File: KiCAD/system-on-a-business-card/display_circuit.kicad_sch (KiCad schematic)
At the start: 12 parts, among them J2 X077-6428TSWCG01-H13, Q1 2N7002K, Q2 BSS84

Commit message: updated documentation, fixed bom export
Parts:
- J2: now in the parts list
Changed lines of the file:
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@@
   )
   (symbol (lib_id "Connector:Conn_01x13_Male") (at 227.33 80.01 0) (mirror y) (unit 1)
-    (in_bom no) (on_board yes)
+    (in_bom yes) (on_board yes)
     (property "Reference" "J2" (id 0) (at 229.87 80.01 0)
       (effects (font (size 1.27 1.27)) (justify right))

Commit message: fixed #12 connected OLED VDD pins to 3.3V power line
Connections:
- net +3.3V: now reaches C19.1, C21.1, J2.4 (Pin_4), J2.5 (Pin_5)

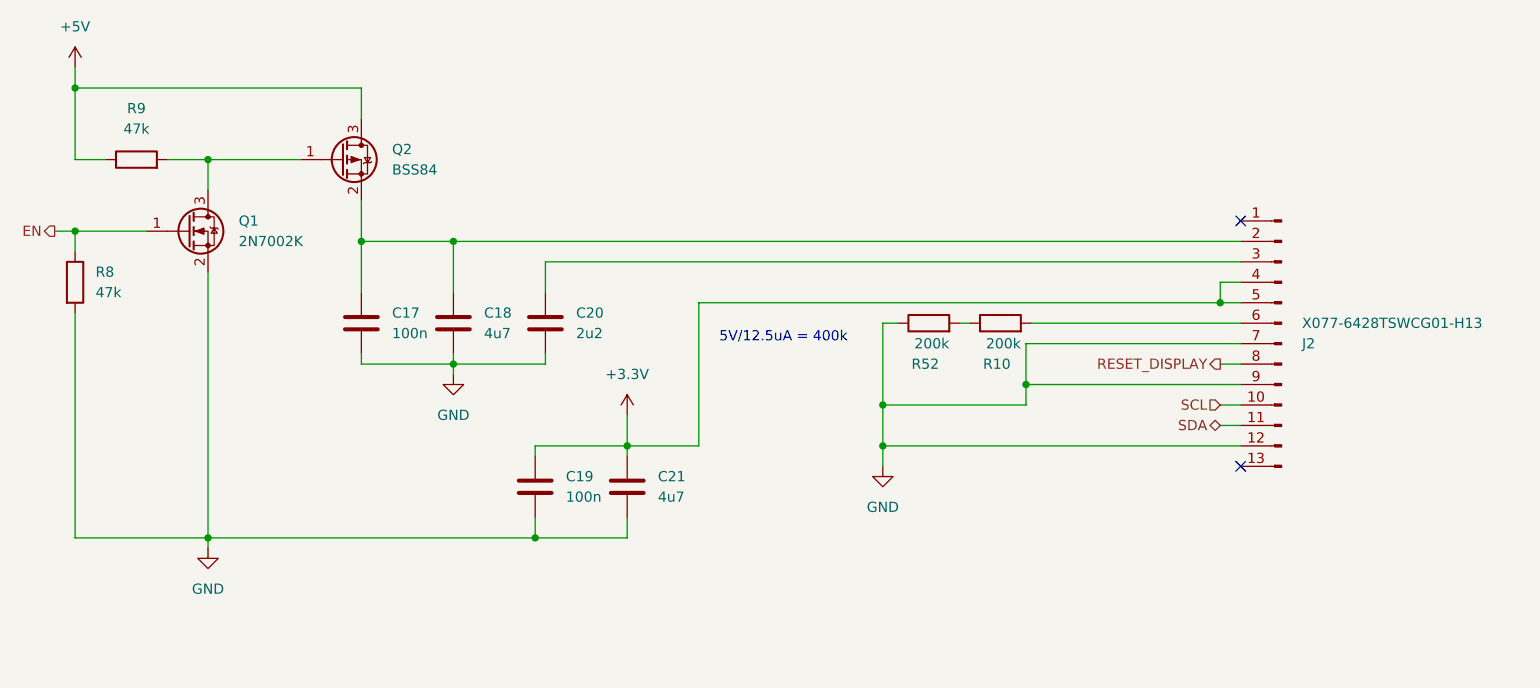
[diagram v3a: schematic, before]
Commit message: #10: added buzzer, io-expander, removed transistors from resistive pad cirucit
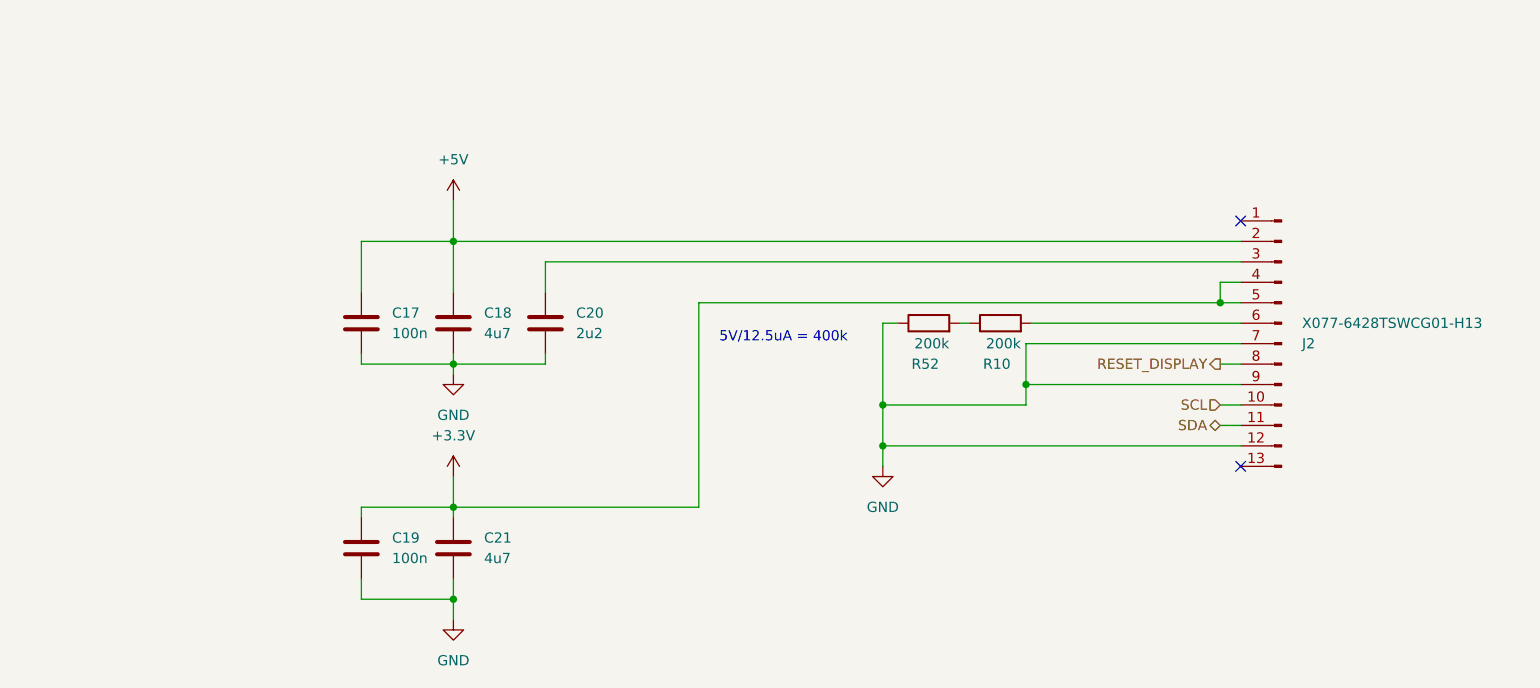
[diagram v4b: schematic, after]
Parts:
- removed Q1: 2N7002K, Package_TO_SOT_SMD:SOT-23, symbol Transistor_FET:2N7002K
- removed Q2: BSS84, Package_TO_SOT_SMD:SOT-23, symbol Transistor_FET:BSS84
- removed R8, R9: 47k, Resistor_SMD:R_0402_1005Metric_Pad0.72x0.64mm_HandSolder, symbol Device:R
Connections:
- net +5V: now also C17.1, C18.1, J2.2 (Pin_2)
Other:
- moved on the sheet: C19, C21

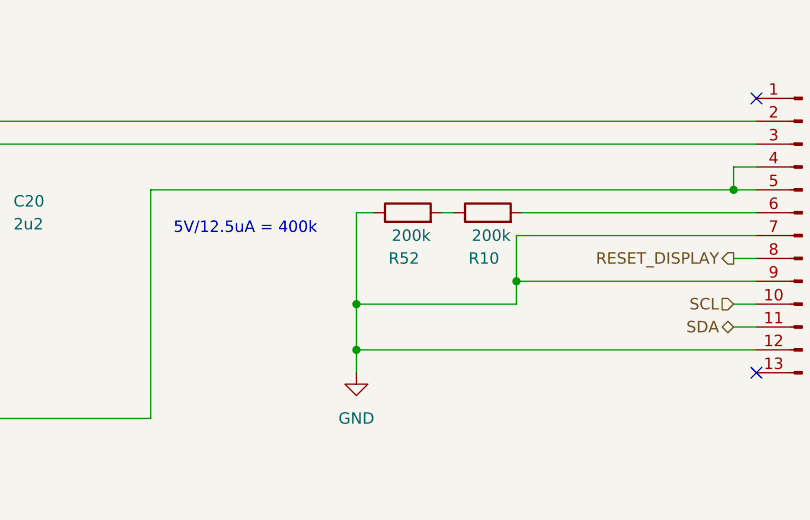
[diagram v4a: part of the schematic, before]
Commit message: #10: removed on/off switch again, started working on layout
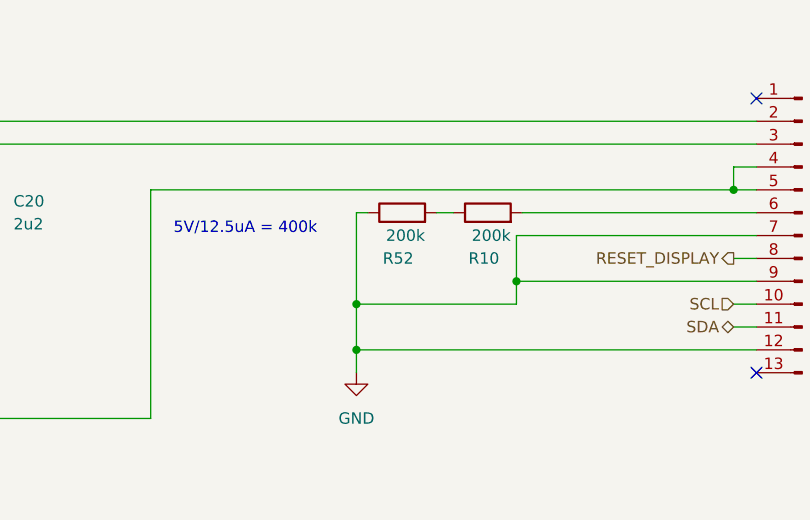
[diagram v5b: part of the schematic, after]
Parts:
- J2: symbol Connector:Conn_01x13_Male -> Connector:Conn_01x13_Pin
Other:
- moved on the sheet: R52
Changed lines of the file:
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@@
     (stroke (width 0) (type default))
   )
-  (wire (pts (xy 177.8 77.47) (xy 179.705 77.47))
+  (wire (pts (xy 177.8 77.47) (xy 179.07 77.47))
     (stroke (width 0) (type default))
   )
@@
     (stroke (width 0) (type default))
   )
-  (wire (pts (xy 187.325 77.47) (xy 188.595 77.47))
+  (wire (pts (xy 186.69 77.47) (xy 188.595 77.47))
     (stroke (width 0) (type default))
   )
@@
     )
   )
-  (symbol (lib_id "Connector:Conn_01x13_Male") (at 227.33 80.01 0) (mirror y) (unit 1)
+  (symbol (lib_id "Connector:Conn_01x13_Pin") (at 227.33 80.01 0) (mirror y) (unit 1)
     (in_bom yes) (on_board yes) (dnp no)
     (property "Reference" "J2" (at 229.87 80.01 0)
@@
     )
   )
-  (symbol (lib_id "Device:R") (at 183.515 77.47 90) (unit 1)
+  (symbol (lib_id "Device:R") (at 182.88 77.47 90) (unit 1)
     (in_bom yes) (on_board yes) (dnp no)
-    (property "Reference" "R52" (at 184.785 82.55 90)
-      (effects (font (size 1.27 1.27)) (justify left))
-    )
-    (property "Value" "200k" (at 186.055 80.01 90)
-      (effects (font (size 1.27 1.27)) (justify left))
-    )
-    (property "Footprint" "Resistor_SMD:R_0402_1005Metric_Pad0.72x0.64mm_HandSolder" (at 183.515 79.248 90)
-      (effects (font (size 1.27 1.27)) hide)
-    )
-    (property "Datasheet" "~" (at 183.515 77.47 0)
-      (effects (font (size 1.27 1.27)) hide)
-    )
+    (property "Reference" "R52" (at 184.15 82.55 90)
+      (effects (font (size 1.27 1.27)) (justify left))
+    )
+    (property "Value" "200k" (at 185.42 80.01 90)
+      (effects (font (size 1.27 1.27)) (justify left))
+    )
+    (property "Footprint" "Resistor_SMD:R_0402_1005Metric_Pad0.72x0.64mm_HandSolder" (at 182.88 79.248 90)
+      (effects (font (size 1.27 1.27)) hide)
+    )
+    (property "Datasheet" "~" (at 182.88 77.47 0)
+      (effects (font (size 1.27 1.27)) hide)
+    )

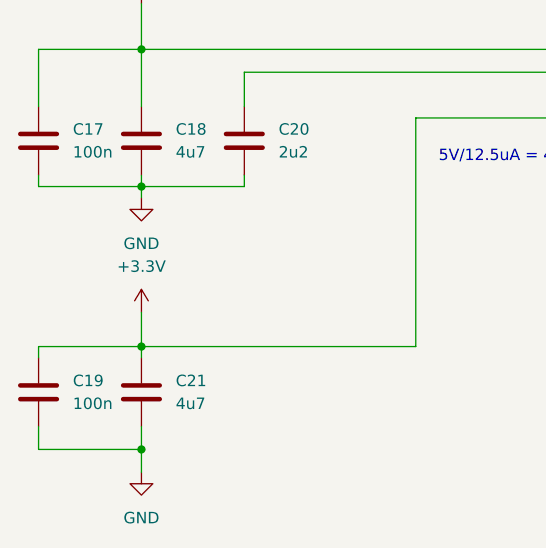
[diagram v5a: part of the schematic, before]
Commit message: #10: mintor tweaks in routing, removed fiducials from bom, added values to buzzer and sd-card slot
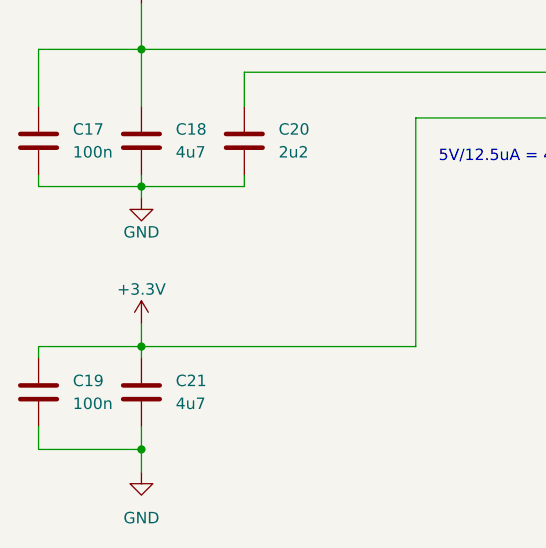
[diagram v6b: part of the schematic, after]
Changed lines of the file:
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@@
     (stroke (width 0) (type default))
   )
-  (wire (pts (xy 124.46 96.52) (xy 124.46 100.33))
+  (wire (pts (xy 124.46 97.79) (xy 124.46 100.33))
     (stroke (width 0) (type default))
   )
@@
   )
   (symbol (lib_id "power:GND") (at 124.46 83.82 0) (unit 1)
-    (in_bom yes) (on_board yes) (dnp no) (fields_autoplaced)
+    (in_bom yes) (on_board yes) (dnp no)
     (property "Reference" "#PWR024" (at 124.46 90.17 0)
       (effects (font (size 1.27 1.27)) hide)
     )
-    (property "Value" "GND" (at 124.46 88.9 0)
+    (property "Value" "GND" (at 124.46 87.63 0)
       (effects (font (size 1.27 1.27)))
     )
@@
     )
   )
-  (symbol (lib_id "power:+3.3V") (at 124.46 96.52 0) (unit 1)
-    (in_bom yes) (on_board yes) (dnp no)
-    (property "Reference" "#PWR04" (at 124.46 100.33 0)
-      (effects (font (size 1.27 1.27)) hide)
-    )
-    (property "Value" "+3.3V" (at 124.46 91.44 0)
+  (symbol (lib_id "power:+3.3V") (at 124.46 97.79 0) (unit 1)
+    (in_bom yes) (on_board yes) (dnp no)
+    (property "Reference" "#PWR04" (at 124.46 101.6 0)
+      (effects (font (size 1.27 1.27)) hide)
+    )
+    (property "Value" "+3.3V" (at 124.46 93.98 0)
       (effects (font (size 1.27 1.27)))
     )
-    (property "Footprint" "" (at 124.46 96.52 0)
-      (effects (font (size 1.27 1.27)) hide)
-    )
-    (property "Datasheet" "" (at 124.46 96.52 0)
-      (effects (font (size 1.27 1.27)) hide)
-    )
+    (property "Footprint" "" (at 124.46 97.79 0)
+      (effects (font (size 1.27 1.27)) hide)
+    )
+    (property "Datasheet" "" (at 124.46 97.79 0)
+      (effects (font (size 1.27 1.27)) hide)
+    )

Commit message: #10: separated reset and display reset signals, added pull-up to display reset
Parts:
- added R5: 5k1, Resistor_SMD:R_0402_1005Metric_Pad0.72x0.64mm_HandSolder, symbol Device:R
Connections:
- net +3.3V: now also R5.1
- net RESET_DISPLAY: now also R5.2
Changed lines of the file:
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@@
   (junction (at 124.46 111.76) (diameter 0) (color 0 0 0 0)
   )
+  (junction (at 154.94 100.33) (diameter 0) (color 0 0 0 0)
+  )
   (junction (at 124.46 82.55) (diameter 0) (color 0 0 0 0)
   )
@@
   )
   (junction (at 124.46 100.33) (diameter 0) (color 0 0 0 0)
+  )
+  (junction (at 154.94 111.76) (diameter 0) (color 0 0 0 0)
   )
   (junction (at 177.8 92.71) (diameter 0) (color 0 0 0 0)
@@
   (no_connect (at 222.25 95.25))
   (no_connect (at 222.25 64.77))
-  (wire (pts (xy 154.94 100.33) (xy 124.46 100.33))
-    (stroke (width 0) (type default))
-  )
   (wire (pts (xy 135.89 69.85) (xy 222.25 69.85))
     (stroke (width 0) (type default))
@@
     (stroke (width 0) (type default))
   )
+  (wire (pts (xy 154.94 111.76) (xy 154.94 110.49))
+    (stroke (width 0) (type default))
+  )
   (wire (pts (xy 113.03 109.22) (xy 113.03 111.76))
     (stroke (width 0) (type default))
@@
     (stroke (width 0) (type default))
   )
+  (wire (pts (xy 124.46 100.33) (xy 154.94 100.33))
+    (stroke (width 0) (type default))
+  )
   (wire (pts (xy 177.8 92.71) (xy 222.25 92.71))
     (stroke (width 0) (type default))
@@
     (stroke (width 0) (type default))
   )
+  (wire (pts (xy 154.94 111.76) (xy 160.02 111.76))
+    (stroke (width 0) (type default))
+  )
   (wire (pts (xy 222.25 80.01) (xy 195.58 80.01))
     (stroke (width 0) (type default))
@@
     (stroke (width 0) (type default))
   )
+  (wire (pts (xy 149.86 111.76) (xy 154.94 111.76))
+    (stroke (width 0) (type default))
+  )
   (wire (pts (xy 195.58 85.09) (xy 222.25 85.09))
     (stroke (width 0) (type default))
@@
   )
   (wire (pts (xy 124.46 62.23) (xy 124.46 67.31))
+    (stroke (width 0) (type default))
+  )
+  (wire (pts (xy 154.94 102.87) (xy 154.94 100.33))
     (stroke (width 0) (type default))
   )
@@
     (effects (font (size 1.27 1.27)) (justify left bottom))
   )
-  (hierarchical_label "RESET_DISPLAY" (shape output) (at 219.71 82.55 180) (fields_autoplaced)
+  (global_label "RESET_DISPLAY" (shape output) (at 160.02 111.76 0) (fields_autoplaced)
+    (effects (font (size 1.27 1.27)) (justify left))
+    (property "Intersheetrefs" "${INTERSHEET_REFS}" (at 177.2775 111.76 0)
+      (effects (font (size 1.27 1.27)) (justify left) hide)
+    )
+  )
+  (global_label "RESET_DISPLAY" (shape output) (at 219.71 82.55 180) (fields_autoplaced)
+    (effects (font (size 1.27 1.27)) (justify right))
+    (property "Intersheetrefs" "${INTERSHEET_REFS}" (at 202.4525 82.55 0)
+      (effects (font (size 1.27 1.27)) (justify right) hide)
+    )
+  )
+  (hierarchical_label "RESET_DISPLAY" (shape output) (at 149.86 111.76 180) (fields_autoplaced)
     (effects (font (size 1.27 1.27)) (justify right))
   )
@@
         )
       )
+    )
+  )
+  (symbol (lib_id "Device:R") (at 154.94 106.68 0) (unit 1)
+    (in_bom yes) (on_board yes) (dnp no) (fields_autoplaced)
+    (property "Reference" "R5" (at 157.48 105.4099 0)
+      (effects (font (size 1.27 1.27)) (justify left))
+    )
+    (property "Value" "5k1" (at 157.48 107.9499 0)
+      (effects (font (size 1.27 1.27)) (justify left))
+    )
+    (property "Footprint" "Resistor_SMD:R_0402_1005Metric_Pad0.72x0.64mm_HandSolder" (at 153.162 106.68 90)
+      (effects (font (size 1.27 1.27)) hide)
+    )
+    (property "Datasheet" "~" (at 154.94 106.68 0)
+      (effects (font (size 1.27 1.27)) hide)
+    )
+    (pin "1")
+    (pin "2")
+    (instances
+      (project "system-on-a-business-card"
+        (path "/49855302-2ecc-4f42-8bbd-b9c2e284f529"
+          (reference "R5") (unit 1)
+        )
+        (path "/49855302-2ecc-4f42-8bbd-b9c2e284f529/ae6d0e78-c13d-437d-adeb-ef8051956add"
+          (reference "R22") (unit 1)
+        )
+      )
